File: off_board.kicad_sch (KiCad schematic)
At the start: 1 part, among them J7 Conn_01x90_3Row_Socket

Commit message: external loops
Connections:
- net B21: no longer J7.51 (B51)
- new net B51: J7.51 (B51)
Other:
- sheet fan_control renamed fan_control_AC
- sheet gas_pcd_valve renamed gas_shut_valves
- sheet injector_valves renamed gasoline_injector
- added sheet cng_switch (cng_switch.kicad_sch)
- added sheet gas_injector (gas_injector.kicad_sch)
- sheet cam_shaft_pos ports: added none; removed B86
- sheet canister_valve ports: added none; removed B29
- sheet communications ports: added B78; removed A64
- sheet fan_control_AC: file fan_control.kicad_sch -> fan_control_AC.kicad_sch
- sheet fan_control_AC ports: added B79; removed A33, B29
- sheet fuel_pump_relay ports: added B80; removed B29, B86
- sheet gas_shut_valves: file blank.kicad_sch -> gas_shut_valves.kicad_sch
- sheet gas_shut_valves ports: added B22; removed B29
- sheet gasoline_injector: file injector_valves.kicad_sch -> gasoline_injector.kicad_sch
- sheet gasoline_injector ports: added none; removed B29, B59, B60, B89, B90
- sheet ignation_coils ports: added none; removed B86
- sheet instrument_cluster ports: added none; removed B29
- sheet oxigen_sensor ports: added none; removed B86
- sheet speed_sensor ports: added none; removed B86
- moved on the sheet: J7A, J7B

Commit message: external loops arrangments1
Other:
- sheet fan_control_AC ports: added A42, A5; removed none

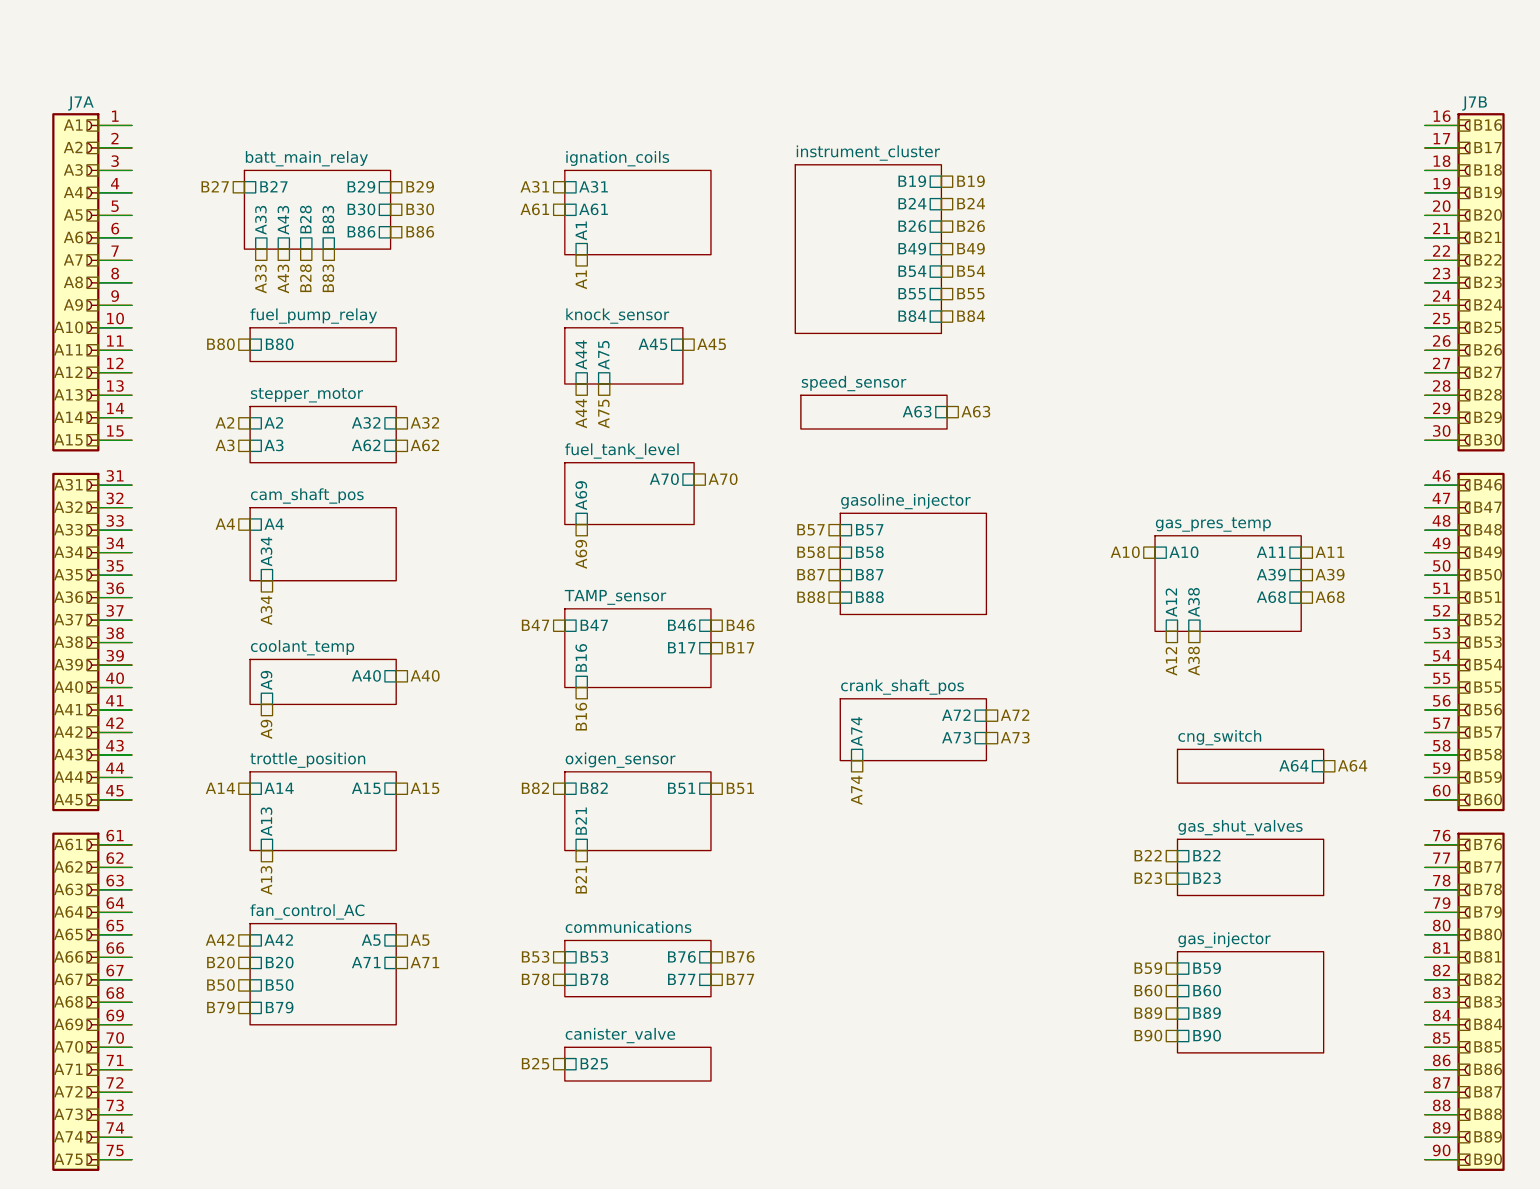
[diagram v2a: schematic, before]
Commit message: air conditioner updated
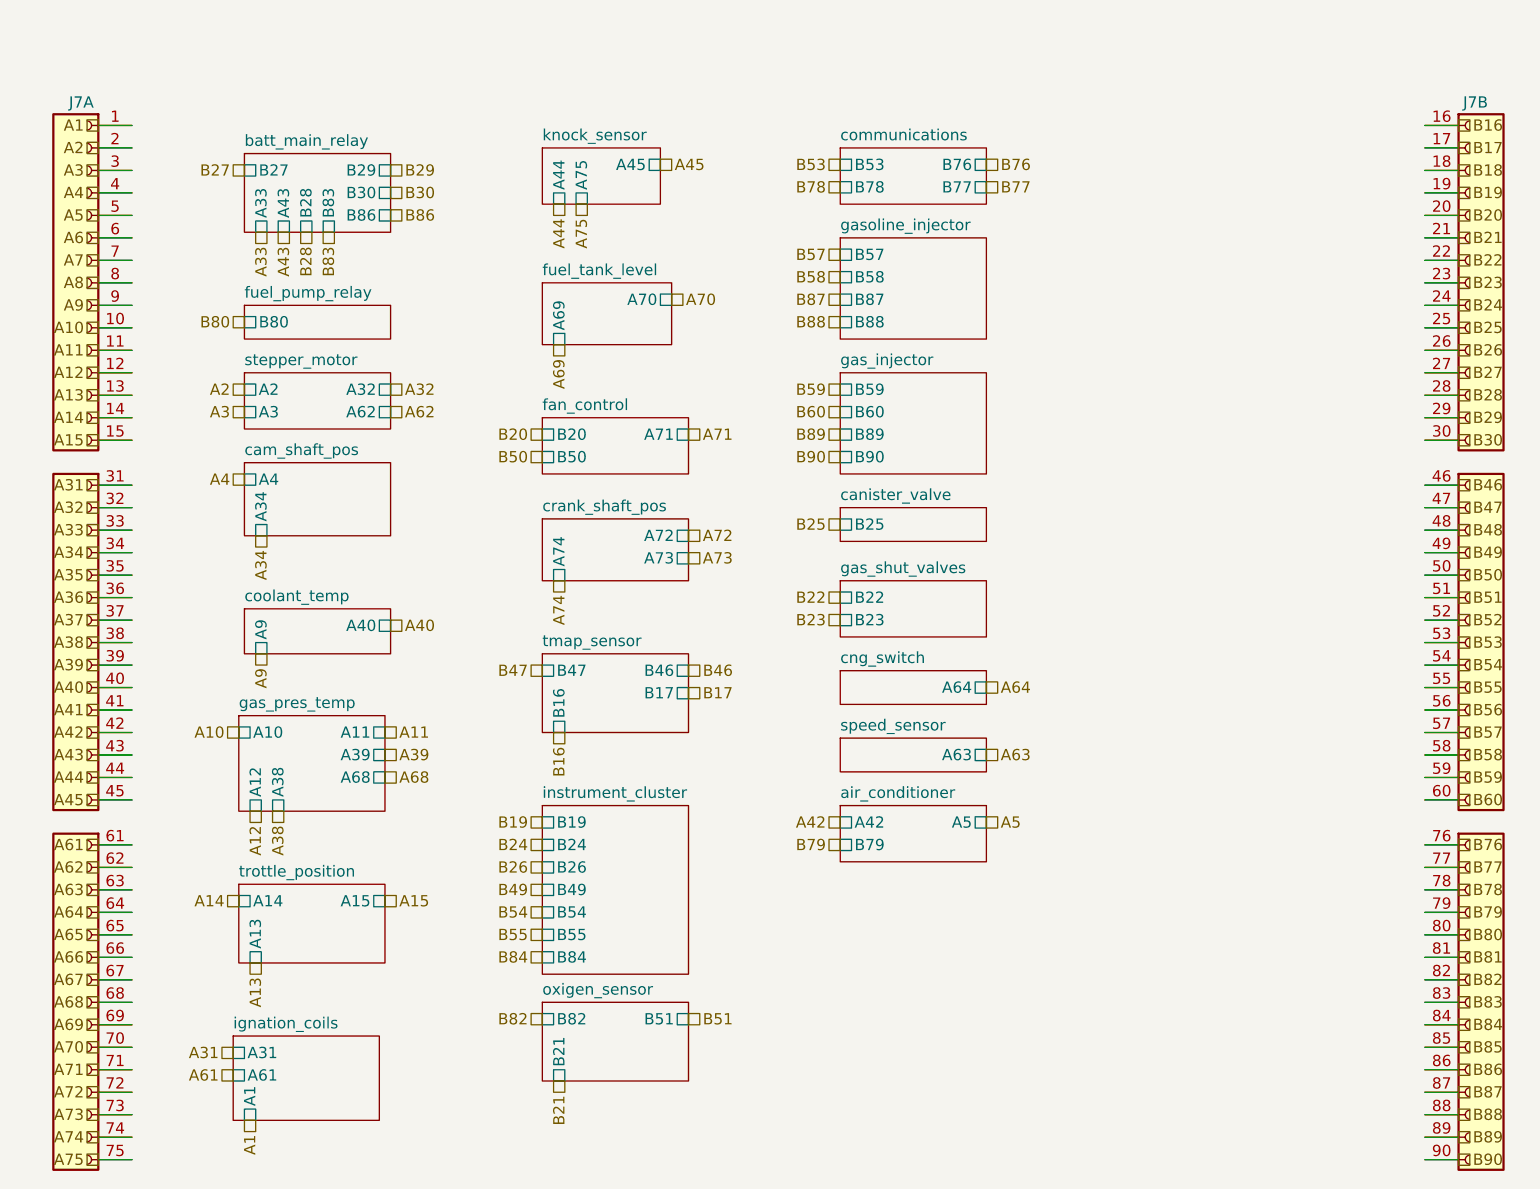
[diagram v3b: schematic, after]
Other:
- sheet TAMP_sensor renamed tmap_sensor
- sheet fan_control_AC renamed fan_control
- added sheet air_conditioner (air_conditioner.kicad_sch)
- sheet fan_control: file fan_control_AC.kicad_sch -> fan_control.kicad_sch
- sheet fan_control ports: added none; removed A42, A5, B79
- sheet tmap_sensor: file TAMP_sensor.kicad_sch -> tmap_sensor.kicad_sch
